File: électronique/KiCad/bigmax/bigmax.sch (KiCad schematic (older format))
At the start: 19 parts, among them SW1 SW_Push, U1 qtr-1rc_a, U10 batt_connector, U2 qtr-1rc_b, U3 dc_geared_encoder, U4 dc_geared_encoder, U5 TPS61090_dc_boost, U6 MT3608, U7 VL53L0X_a, U8 VL53L0X_b, U9 dc_driver_1A_3-14V

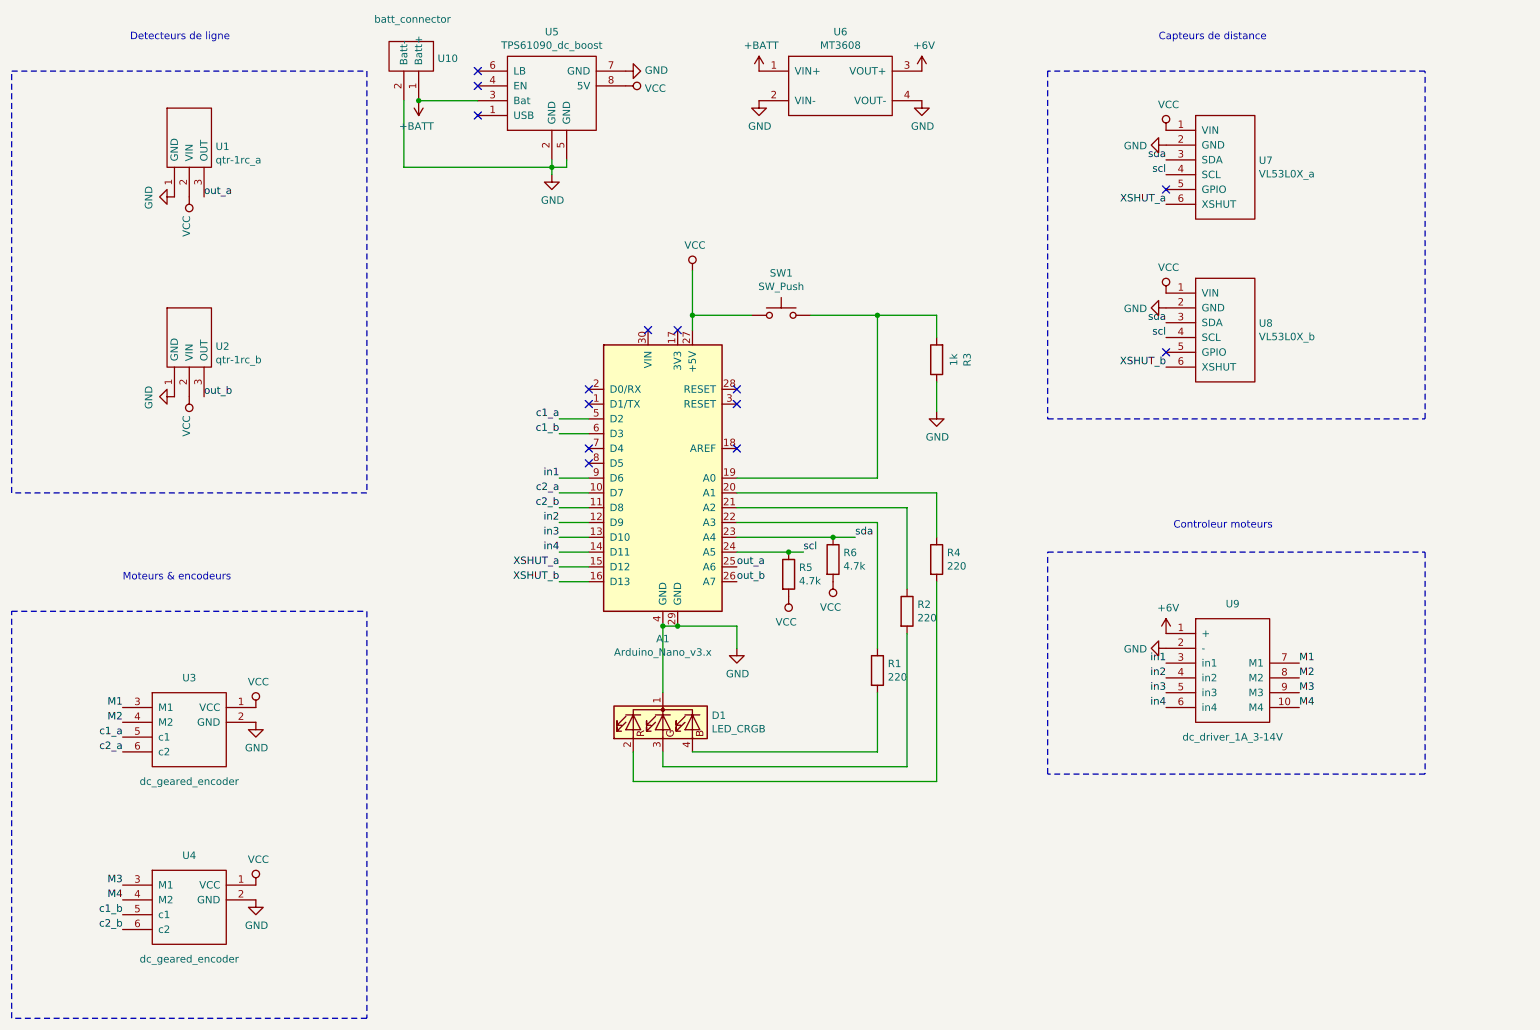
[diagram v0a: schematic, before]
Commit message: mise à jour du projet kicad en ajoutant des résistances de pull-up sur la commande des moteurs et une capacité de découplage en entrée du controller moteurs
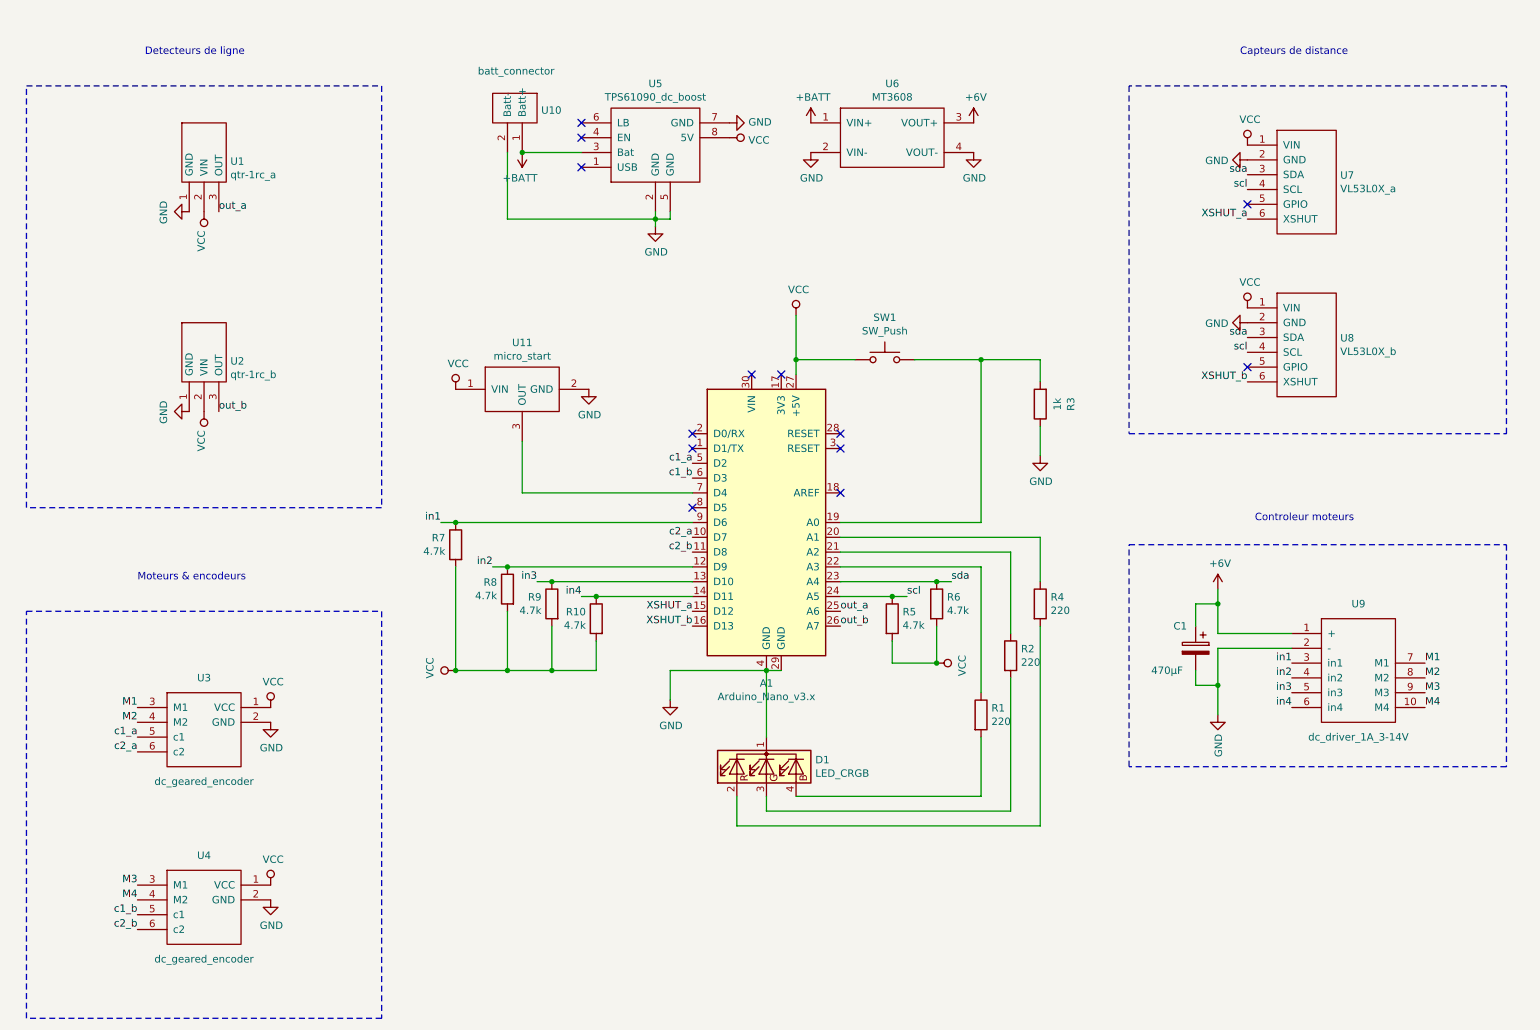
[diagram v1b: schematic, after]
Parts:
- added C1: 470µF, Capacitors_THT:CP_Radial_D10.0mm_P5.00mm, symbol Device:CP
- added R10, R7, R8, R9: 4.7k, Resistors_THT:R_Axial_DIN0207_L6.3mm_D2.5mm_P10.16mm_Horizontal, symbol Device:R
- added U11: micro_start, bigmax:micro_start, symbol bigmax:micro_start
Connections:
- net +6V: now also C1.1
- net GND: now also C1.2, U11.2 (GND)
- net VCC: now also R10.2, R7.2, R8.2, R9.2, U11.1 (VIN)
- net in1: now also R7.1
- net in2: now also R8.1
- net in3: now also R9.1
- net in4: now also R10.1
- net at A1.7 (D4): now also U11.3 (OUT)
- no-connect marks 14 -> 13
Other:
- moved on the sheet: A1, D1, R1, R2, R3, R4, R5, R6, SW1, U1, U10, U2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

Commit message: Bigmax v2 - mai 2019
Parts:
- removed U1: qtr-1rc_a, bigmax:qtr_1rc, symbol bigmax:QTR-1RC
- removed U10: batt_connector, bigmax:batt_connector, symbol bigmax:batt_connector
- removed U11: micro_start, bigmax:micro_start, symbol bigmax:micro_start
- removed U2: qtr-1rc_b, bigmax:qtr_1rc, symbol bigmax:QTR-1RC
- removed U3, U4: dc_geared_encoder, bigmax:dc_geared_encoder, symbol bigmax:dc_motor_encoder
- removed U5: TPS61090_dc_boost, bigmax:dc_boost_500C, symbol bigmax:TPS61090_dc_boost
- removed U6: MT3608, bigmax:MT3608, symbol bigmax:MT3608
- removed U7: VL53L0X_a, bigmax:vl53l0x, symbol bigmax:VL53L0X
- removed U8: VL53L0X_b, bigmax:vl53l0x, symbol bigmax:VL53L0X
- removed U9: dc_driver_1A_3-14V, bigmax:MX1616, symbol bigmax:dc_driver_1A_3-14V
- added J1: Conn_01x03, Pin_Headers:Pin_Header_Angled_1x03_Pitch2.54mm, symbol no_name:Conn_01x03_output
- added J2, J4: Conn_01x02, Pin_Headers:Pin_Header_Angled_1x02_Pitch2.54mm, symbol no_name:Conn_01x02
- added J3: Conn_01x03_input, Pin_Headers:Pin_Header_Angled_1x03_Pitch2.54mm, symbol no_name:Conn_01x03_input
- added U1, U2: pololu_enc03b, bigmax:pololu_enc03b, symbol pololu:pololu_enc03b
- added U10: jsumo_micro_start, bigmax:jsumo_micro_start, symbol jsumo:jsumo_micro_start
- added U11: generic_vertical_slide_switch, Pin_Headers:Pin_Header_Straight_1x03_Pitch2.54mm, symbol no_name:generic_vertical_slide_switch
- added U12: generic_bms_3s_10A, bigmax:generic_bms_3s_10A, symbol no_name:generic_bms_3s_10A
- added U13: generic_18650_3s_case, bigmax:CB-18650-PC6, symbol no_name:generic_18650_3s_case
- added U3, U4: pololu_irs01a, bigmax:pololu_irs01a, symbol pololu:pololu_irs01a
- added U5: pololu_reg19a, bigmax:pololu_reg19a, symbol pololu:pololu_reg19a
- added U6: pololu_reg04b, bigmax:pololu_reg04b, symbol pololu:pololu_reg04b
- added U7: pololu_md17a, bigmax:pololu_md17a, symbol pololu:pololu_md17a
- added U8, U9: generic_vl53l0x, bigmax:generic_vl53l0x, symbol no_name:generic_vl53l0x
- A1: symbol bigmax:Arduino_Nano_v3.x -> arduino:Arduino_Nano_v3.x
- D1: footprint LEDs:LED_D5.0mm-4 -> bigmax:LED_D5.0mm-4; symbol Device:LED_CRGB -> Device:LED_RCGB
- renumbered R5 to R10, R4 to R3, R3 to R4, R6 to R5, R7 to R6, R8 to R7, R9 to R8, R10 to R9
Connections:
- net +6V: now also U5.5 (out), U7.10 (vin)
- net GND: now also D1.2 (K), J1.1 (Pin_1), J2.1 (Pin_1), U1.1 (gnd), U2.1 (gnd), U3.1 (gnd), U4.1 (gnd), U5.4 (gnd), U5.6 (gnd), U6.2 (gnd), U7.1 (gnd), U7.9 (gnd), U8.2 (gnd), U9.2 (gnd); no longer D1.1 (K)
- net M1: now also U1.6 (M1), U7.14 (out_a1)
- net M2: now also U1.5 (M2), U7.13 (out_a2)
- net M3: now also U2.6 (M1), U7.11 (out_b1)
- net M4: now also U2.5 (M2), U7.12 (out_b2)
- net XSHUT_a: now also U8.6 (xshut)
- net XSHUT_b: now also U9.6 (xshut)
- net c1_a: now also U1.3 (a)
- net c1_b: now also U2.3 (a)
- net c2_a: now also U1.2 (b)
- net c2_b: now also U2.2 (b)
- net in1: now also R9.1, U7.6 (in_a1); no longer R6.1
- net in2: now also R8.1, U7.5 (in_a2); no longer R7.1
- net in3: now also R6.1, U7.3 (in_b1); no longer R8.1
- net in4: now also R7.1, U7.4 (in_b2); no longer R9.1
- net out_a: now also U3.3 (out)
- net out_b: now also U4.3 (out)
- net scl: now also R10.2, U8.3 (scl), U9.3 (scl); no longer R10.1
- net sda: now also R5.2, U8.4 (sda), U9.4 (sda); no longer R5.1
- net at A1.19 (A0), R4.2: now also SW1.1; no longer SW1.2
- net led_red: now reaches A1.20 (A1), R3.1
- net led_green: now reaches A1.21 (A2), R2.1
- net led_blue: now reaches A1.22 (A3), R1.1
- net +12V: now reaches A1.30 (VIN)
- net +12V: now also J2.2 (Pin_2), U5.3 (in), U6.3 (vin)
- net at A1.7 (D4): now also J1.2 (Pin_2)
- net at R3.2: now also D1.1 (RA); no longer D1.2 (RA)
- net VCC renamed +5V
- net +5V: now also R10.1, R5.1, SW1.2, J1.3 (Pin_3), U1.4 (vcc), U2.4 (vcc), U3.2 (vin), U4.2 (vin), U6.1 (vout), U8.1 (vin), U9.1 (vin); no longer A1.27 (+5V), R10.2, R5.2, SW1.1
- new net: J3.3 (Pin_3), U10.1 (VIN)
- new net: J3.1 (Pin_1), U10.2 (GND)
- new net: J3.2 (Pin_2), U10.3 (OUT)
- new net: J4.2 (Pin_2), U11.1
- new net: U11.2, U12.1 (p+)
- new net: J4.1 (Pin_1), U12.2 (p-)
- new net b+: U12.3 (b+), U13.1 (+)
- new net b-: U12.6 (b-), U13.6 (-)
- new net b1: U12.4 (b1), U13.3 (+), U13.5 (-)
- new net b2: U12.5 (b2), U13.2 (+), U13.4 (-)
- no-connect marks 13 -> 19
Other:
- note added: "Adaptation des tensions 5V et 6V"
- note added: "Alimentation batterie et protection électrique"
- note added: "DEL de status"
- note added: "micro_start jsumo"
- moved on the sheet: A1, C1, R1, R10, R2, R3, R4, R5, R6, R7, R8, R9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
